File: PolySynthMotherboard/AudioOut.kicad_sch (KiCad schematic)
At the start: 19 parts, among them J801 AUDIO_OUT, U801 TL074

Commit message: board layout
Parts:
- R360: value 1k -> 470
- U801: footprint PCM_Package_SO_AKL:SOIC-14_3.9x8.7mm_P1.27mm -> Package_SO:SOIC-14_3.9x8.7mm_P1.27mm
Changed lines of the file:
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@@
       (effects (font (size 1.27 1.27)))
     )
-    (property "Footprint" "PCM_Package_SO_AKL:SOIC-14_3.9x8.7mm_P1.27mm" (at 133.477 70.485 0)
+    (property "Footprint" "Package_SO:SOIC-14_3.9x8.7mm_P1.27mm" (at 133.477 70.485 0)
       (effects (font (size 1.27 1.27)) hide)
     )
@@
       (effects (font (size 1.27 1.27)))
     )
-    (property "Footprint" "PCM_Package_SO_AKL:SOIC-14_3.9x8.7mm_P1.27mm" (at 132.588 110.617 0)
+    (property "Footprint" "Package_SO:SOIC-14_3.9x8.7mm_P1.27mm" (at 132.588 110.617 0)
       (effects (font (size 1.27 1.27)) hide)
     )
@@
       (effects (font (size 1.27 1.27)) (justify right))
     )
-    (property "Footprint" "PCM_Package_SO_AKL:SOIC-14_3.9x8.7mm_P1.27mm" (at 46.863 123.317 0)
+    (property "Footprint" "Package_SO:SOIC-14_3.9x8.7mm_P1.27mm" (at 46.863 123.317 0)
       (effects (font (size 1.27 1.27)) hide)
     )
@@
   (symbol (lib_id "Device:R_US") (at 147.447 108.077 90) (unit 1)
     (in_bom yes) (on_board yes) (dnp no) (fields_autoplaced)
-    (property "Reference" "R360" (at 147.447 101.727 90)
-      (effects (font (size 1.27 1.27)))
-    )
-    (property "Value" "1k" (at 147.447 104.267 90)
+    (property "Reference" "R360" (at 147.447 102.87 90)
+      (effects (font (size 1.27 1.27)))
+    )
+    (property "Value" "470" (at 147.447 105.41 90)
       (effects (font (size 1.27 1.27)))
     )
@@
   (symbol (lib_id "Device:R_US") (at 147.955 67.945 90) (unit 1)
     (in_bom yes) (on_board yes) (dnp no) (fields_autoplaced)
-    (property "Reference" "R360" (at 147.955 61.595 90)
-      (effects (font (size 1.27 1.27)))
-    )
-    (property "Value" "1k" (at 147.955 64.135 90)
+    (property "Reference" "R360" (at 147.955 62.23 90)
+      (effects (font (size 1.27 1.27)))
+    )
+    (property "Value" "470" (at 147.955 64.77 90)
       (effects (font (size 1.27 1.27)))
     )
@@
       (effects (font (size 1.27 1.27)))
     )
-    (property "Footprint" "PCM_Package_SO_AKL:SOIC-14_3.9x8.7mm_P1.27mm" (at 87.249 122.555 0)
+    (property "Footprint" "Package_SO:SOIC-14_3.9x8.7mm_P1.27mm" (at 87.249 122.555 0)
       (effects (font (size 1.27 1.27)) hide)
     )
@@
       (effects (font (size 1.27 1.27)))
     )
-    (property "Footprint" "PCM_Package_SO_AKL:SOIC-14_3.9x8.7mm_P1.27mm" (at 76.581 60.325 0)
-      (effects (font (size 1.27 1.27)) hide)
-    )
+    (property "Footprint" "Package_SO:SOIC-14_3.9x8.7mm_P1.27mm" (at 76.581 60.325 0)
+      (effects (font (size 1.27 1.27)) hide)
+    )

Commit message: new voice board proj
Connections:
- net AUDIO_OUT_R renamed AUDIO_OUT_L
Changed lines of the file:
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@@
     )
   )
-  (global_label "AUDIO_OUT_R" (shape output) (at 154.305 108.077 0) (fields_autoplaced)
+  (global_label "AUDIO_OUT_L" (shape output) (at 154.305 108.077 0) (fields_autoplaced)
     (effects (font (size 1.27 1.27)) (justify left))
     (property "Intersheetrefs" "${INTERSHEET_REFS}" (at 169.7484 108.077 0)

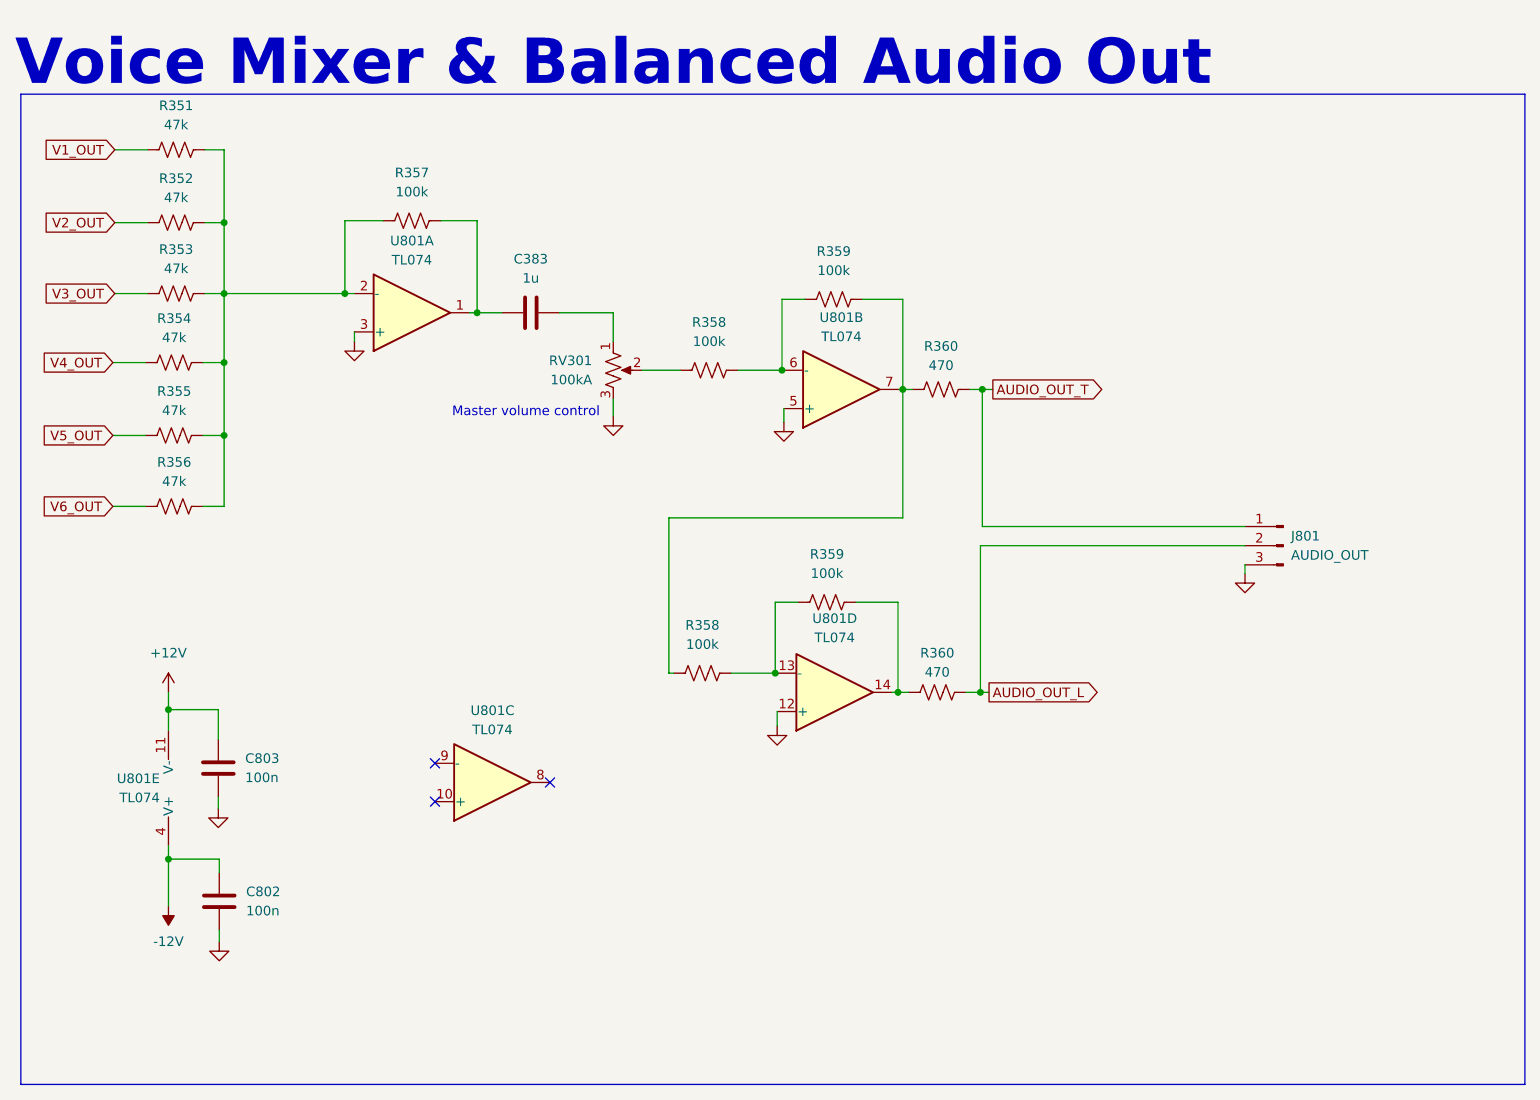
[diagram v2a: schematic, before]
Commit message: cleaned up CV opamps
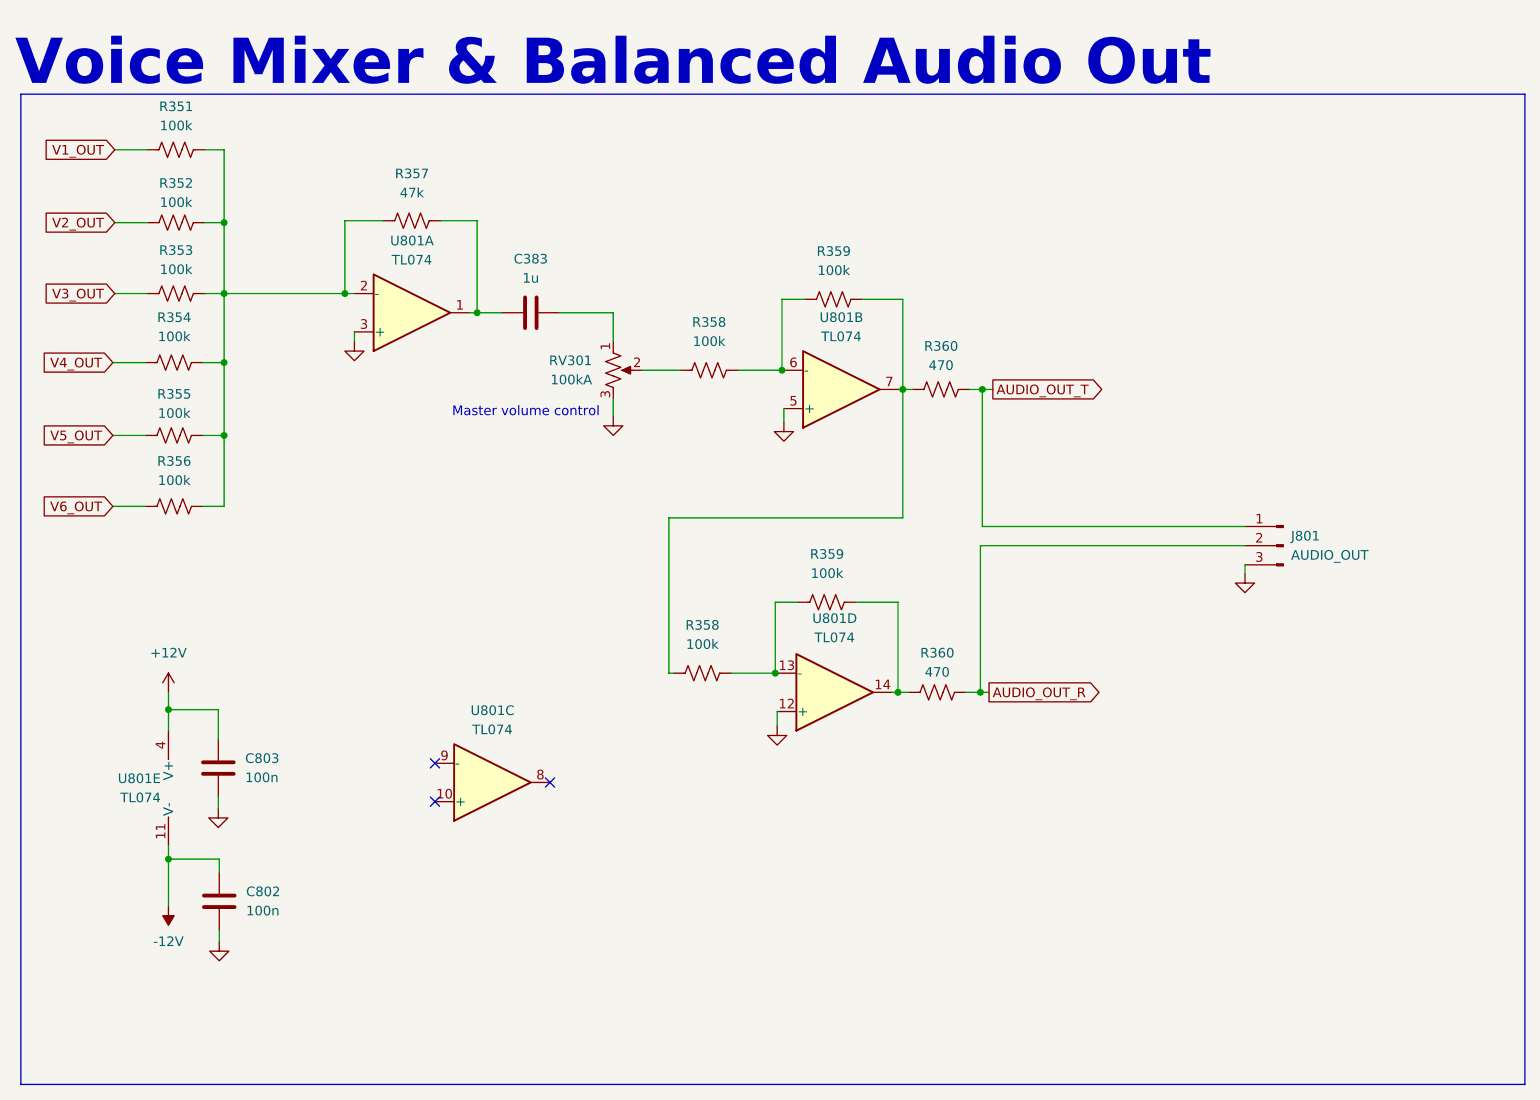
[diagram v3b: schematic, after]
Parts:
- R351, R352, R353, R354, R355, R356: value 47k -> 100k
- R357: value 100k -> 47k
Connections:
- net +12V: now also U801.4 (V+); no longer U801.11 (V-)
- net -12V: now also U801.11 (V-); no longer U801.4 (V+)
- net AUDIO_OUT_L renamed AUDIO_OUT_R
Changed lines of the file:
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@@
     )
   )
-  (global_label "AUDIO_OUT_L" (shape output) (at 154.305 108.077 0) (fields_autoplaced)
+  (global_label "AUDIO_OUT_R" (shape output) (at 154.305 108.077 0) (fields_autoplaced)
     (effects (font (size 1.27 1.27)) (justify left))
     (property "Intersheetrefs" "${INTERSHEET_REFS}" (at 169.7484 108.077 0)
@@
   (symbol (lib_id "Device:R_US") (at 46.355 83.439 90) (unit 1)
     (in_bom yes) (on_board yes) (dnp no) (fields_autoplaced)
-    (property "Reference" "R356" (at 46.355 77.597 90)
-      (effects (font (size 1.27 1.27)))
-    )
-    (property "Value" "47k" (at 46.355 80.137 90)
+    (property "Reference" "R356" (at 46.355 77.47 90)
+      (effects (font (size 1.27 1.27)))
+    )
+    (property "Value" "100k" (at 46.355 80.01 90)
       (effects (font (size 1.27 1.27)))
     )
@@
   (symbol (lib_id "Device:R_US") (at 46.609 36.195 90) (unit 1)
     (in_bom yes) (on_board yes) (dnp no) (fields_autoplaced)
-    (property "Reference" "R351" (at 46.609 30.353 90)
-      (effects (font (size 1.27 1.27)))
-    )
-    (property "Value" "47k" (at 46.609 32.893 90)
+    (property "Reference" "R351" (at 46.609 30.48 90)
+      (effects (font (size 1.27 1.27)))
+    )
+    (property "Value" "100k" (at 46.609 33.02 90)
       (effects (font (size 1.27 1.27)))
     )
@@
   (symbol (lib_id "Device:R_US") (at 46.609 45.847 90) (unit 1)
     (in_bom yes) (on_board yes) (dnp no) (fields_autoplaced)
-    (property "Reference" "R352" (at 46.609 40.005 90)
-      (effects (font (size 1.27 1.27)))
-    )
-    (property "Value" "47k" (at 46.609 42.545 90)
+    (property "Reference" "R352" (at 46.609 40.64 90)
+      (effects (font (size 1.27 1.27)))
+    )
+    (property "Value" "100k" (at 46.609 43.18 90)
       (effects (font (size 1.27 1.27)))
     )
@@
   (symbol (lib_id "Device:R_US") (at 46.355 74.041 90) (unit 1)
     (in_bom yes) (on_board yes) (dnp no) (fields_autoplaced)
-    (property "Reference" "R355" (at 46.355 68.199 90)
-      (effects (font (size 1.27 1.27)))
-    )
-    (property "Value" "47k" (at 46.355 70.739 90)
+    (property "Reference" "R355" (at 46.355 68.58 90)
+      (effects (font (size 1.27 1.27)))
+    )
+    (property "Value" "100k" (at 46.355 71.12 90)
       (effects (font (size 1.27 1.27)))
     )
@@
   (symbol (lib_id "Device:R_US") (at 46.609 55.245 90) (unit 1)
     (in_bom yes) (on_board yes) (dnp no) (fields_autoplaced)
-    (property "Reference" "R353" (at 46.609 49.403 90)
-      (effects (font (size 1.27 1.27)))
-    )
-    (property "Value" "47k" (at 46.609 51.943 90)
+    (property "Reference" "R353" (at 46.609 49.53 90)
+      (effects (font (size 1.27 1.27)))
+    )
+    (property "Value" "100k" (at 46.609 52.07 90)
       (effects (font (size 1.27 1.27)))
     )
@@
     )
   )
-  (symbol (lib_id "Amplifier_Operational:TL074") (at 48.133 120.777 0) (mirror x) (unit 5)
-    (in_bom yes) (on_board yes) (dnp no) (fields_autoplaced)
-    (property "Reference" "U801" (at 44.45 119.507 0)
+  (symbol (lib_id "Amplifier_Operational:TL074") (at 48.133 120.777 0) (unit 5)
+    (in_bom yes) (on_board yes) (dnp no)
+    (property "Reference" "U801" (at 44.577 119.507 0)
       (effects (font (size 1.27 1.27)) (justify right))
     )
-    (property "Value" "TL074" (at 44.45 122.047 0)
+    (property "Value" "TL074" (at 44.577 122.047 0)
       (effects (font (size 1.27 1.27)) (justify right))
     )
-    (property "Footprint" "Package_SO:SOIC-14_3.9x8.7mm_P1.27mm" (at 46.863 123.317 0)
-      (effects (font (size 1.27 1.27)) hide)
-    )
-    (property "Datasheet" "http://www.ti.com/lit/ds/symlink/tl071.pdf" (at 49.403 125.857 0)
+    (property "Footprint" "Package_SO:SOIC-14_3.9x8.7mm_P1.27mm" (at 46.863 118.237 0)
+      (effects (font (size 1.27 1.27)) hide)
+    )
+    (property "Datasheet" "http://www.ti.com/lit/ds/symlink/tl071.pdf" (at 49.403 115.697 0)
       (effects (font (size 1.27 1.27)) hide)
     )
@@
   (symbol (lib_id "Device:R_US") (at 77.851 45.593 90) (unit 1)
     (in_bom yes) (on_board yes) (dnp no) (fields_autoplaced)
-    (property "Reference" "R357" (at 77.851 39.243 90)
-      (effects (font (size 1.27 1.27)))
-    )
-    (property "Value" "100k" (at 77.851 41.783 90)
+    (property "Reference" "R357" (at 77.851 39.37 90)
+      (effects (font (size 1.27 1.27)))
+    )
+    (property "Value" "47k" (at 77.851 41.91 90)
       (effects (font (size 1.27 1.27)))
     )
@@
   (symbol (lib_id "Device:R_US") (at 46.355 64.389 90) (unit 1)
     (in_bom yes) (on_board yes) (dnp no) (fields_autoplaced)
-    (property "Reference" "R354" (at 46.355 58.547 90)
-      (effects (font (size 1.27 1.27)))
-    )
-    (property "Value" "47k" (at 46.355 61.087 90)
-      (effects (font (size 1.27 1.27)))
-    )
+    (property "Reference" "R354" (at 46.355 58.42 90)
+      (effects (font (size 1.27 1.27)))
+    )
+    (property "Value" "100k" (at 46.355 60.96 90)
+      (effects (font (size 1.27 1.27)))
+    )

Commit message: updated to kicad 8
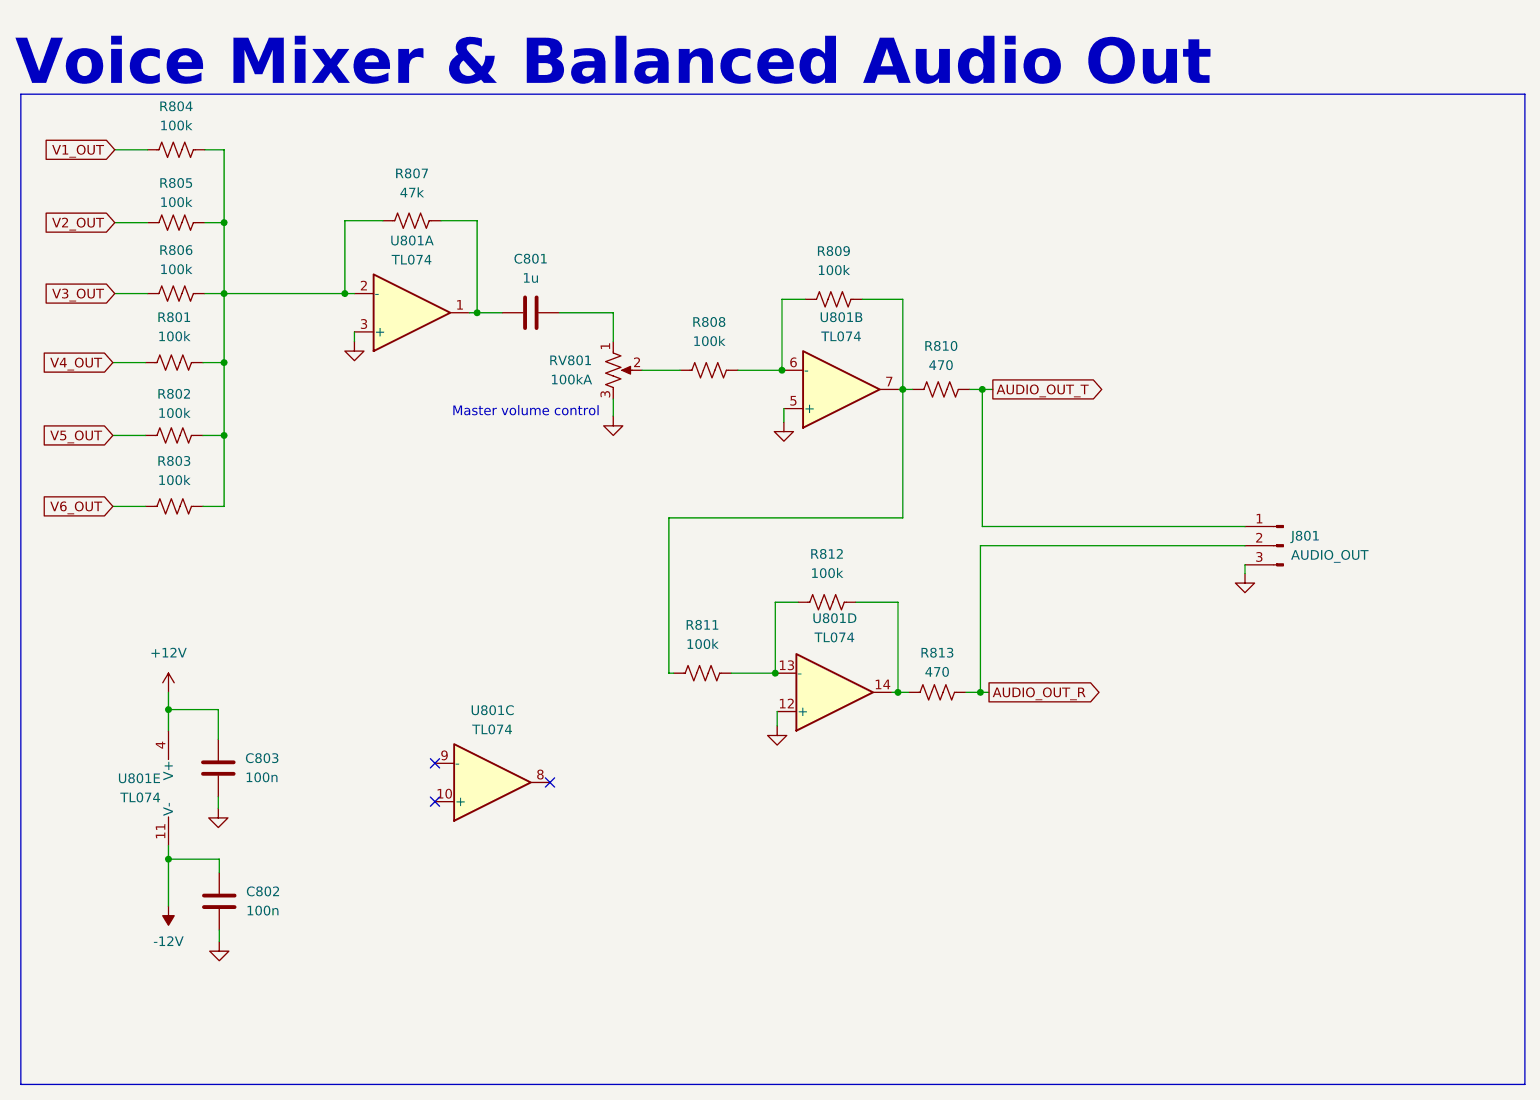
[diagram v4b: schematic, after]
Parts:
- renumbered C383 to C801, R354 to R801, R355 to R802, R356 to R803, R351 to R804, R352 to R805, R353 to R806, R357 to R807, R358 to R808, R359 to R809, R360 to R810, R358 to R811, R359 to R812, R360 to R813, RV301 to RV801

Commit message: fixed footprints, switched optocoupler
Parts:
- R801, R802, R803, R804, R805, R806, R807, R808, R809, R810, R811, R812, R813: footprint PCM_Resistor_SMD_AKL:R_0805_2012Metric -> Resistor_SMD:R_0805_2012Metric
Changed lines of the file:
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@@
 			)
 		)
-		(property "Footprint" "PCM_Resistor_SMD_AKL:R_0805_2012Metric"
+		(property "Footprint" "Resistor_SMD:R_0805_2012Metric"
 			(at 133.985 54.991 90)
 			(effects
@@
 			)
 		)
-		(property "Footprint" "PCM_Resistor_SMD_AKL:R_0805_2012Metric"
+		(property "Footprint" "Resistor_SMD:R_0805_2012Metric"
 			(at 46.609 82.423 90)
 			(effects
@@
 			)
 		)
-		(property "Footprint" "PCM_Resistor_SMD_AKL:R_0805_2012Metric"
+		(property "Footprint" "Resistor_SMD:R_0805_2012Metric"
 			(at 46.863 35.179 90)
 			(effects
@@
 			)
 		)
-		(property "Footprint" "PCM_Resistor_SMD_AKL:R_0805_2012Metric"
+		(property "Footprint" "Resistor_SMD:R_0805_2012Metric"
 			(at 46.863 44.831 90)
 			(effects
@@
 			)
 		)
-		(property "Footprint" "PCM_Resistor_SMD_AKL:R_0805_2012Metric"
+		(property "Footprint" "Resistor_SMD:R_0805_2012Metric"
 			(at 133.096 95.123 90)
 			(effects
@@
 			)
 		)
-		(property "Footprint" "PCM_Resistor_SMD_AKL:R_0805_2012Metric"
+		(property "Footprint" "Resistor_SMD:R_0805_2012Metric"
 			(at 46.609 73.025 90)
 			(effects
@@
 			)
 		)
-		(property "Footprint" "PCM_Resistor_SMD_AKL:R_0805_2012Metric"
+		(property "Footprint" "Resistor_SMD:R_0805_2012Metric"
 			(at 46.863 54.229 90)
 			(effects
@@
 			)
 		)
-		(property "Footprint" "PCM_Resistor_SMD_AKL:R_0805_2012Metric"
+		(property "Footprint" "Resistor_SMD:R_0805_2012Metric"
 			(at 117.475 64.389 90)
 			(effects
@@
 			)
 		)
-		(property "Footprint" "PCM_Resistor_SMD_AKL:R_0805_2012Metric"
+		(property "Footprint" "Resistor_SMD:R_0805_2012Metric"
 			(at 116.586 104.521 90)
 			(effects
@@
 			)
 		)
-		(property "Footprint" "PCM_Resistor_SMD_AKL:R_0805_2012Metric"
+		(property "Footprint" "Resistor_SMD:R_0805_2012Metric"
 			(at 147.701 107.061 90)
 			(effects
@@
 			)
 		)
-		(property "Footprint" "PCM_Resistor_SMD_AKL:R_0805_2012Metric"
+		(property "Footprint" "Resistor_SMD:R_0805_2012Metric"
 			(at 148.209 66.929 90)
 			(effects
@@
 			)
 		)
-		(property "Footprint" "PCM_Resistor_SMD_AKL:R_0805_2012Metric"
+		(property "Footprint" "Resistor_SMD:R_0805_2012Metric"
 			(at 78.105 44.577 90)
 			(effects
@@
 			)
 		)
-		(property "Footprint" "PCM_Resistor_SMD_AKL:R_0805_2012Metric"
+		(property "Footprint" "Resistor_SMD:R_0805_2012Metric"
 			(at 46.609 63.373 90)
 			(effects

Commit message: board iteration
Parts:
- RV801: footprint PCM_Potentiometer_THT_AKL_Double:Potentiometer_Alps_RK09K_Single_Vertical -> Potentiometer_THT:Potentiometer_Bourns_PTV09A-1_Single_Vertical
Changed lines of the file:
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@@
 			)
 		)
-		(property "Footprint" "PCM_Potentiometer_THT_AKL_Double:Potentiometer_Alps_RK09K_Single_Vertical"
+		(property "Footprint" "Potentiometer_THT:Potentiometer_Bourns_PTV09A-1_Single_Vertical"
 			(at 104.521 65.405 0)
 			(effects
